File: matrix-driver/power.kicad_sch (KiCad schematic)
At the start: 28 parts, among them IC1 SPX5205M5-L-3-3_TR, U1 TPS562202, U3 TPS562202

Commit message: added gerbers and finalized v1.0
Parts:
- C12, C13: value 22uF -> 33uF
- C14: value 10nF -> 10pF; now not fitted
- C7: value 10nF -> 22pF
- IC1: DigiKey Part Number (none) -> 1016-1878-2-ND
- L1, L2: footprint (none) -> ETQ_P3M3R3KVP:IND_PCC-M0530M-LP_PAN
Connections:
- net +12V: now also C17.1, IC1.1 (VIN), IC1.3 (EN)

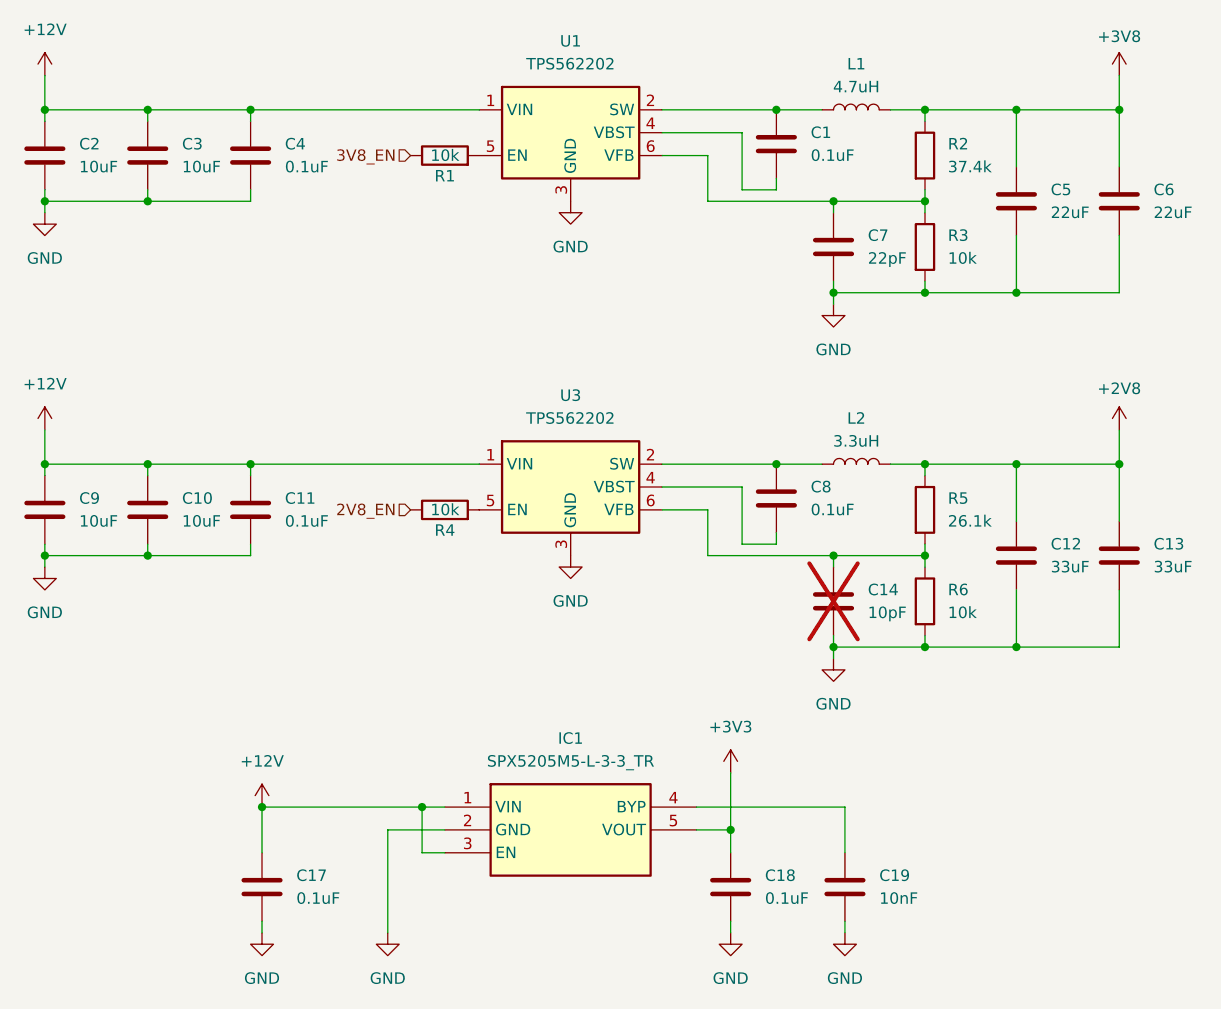
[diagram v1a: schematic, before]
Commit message: changed to through hole connectors for matrix drive unit and updated schematic to reflect thermistors and reserved pin
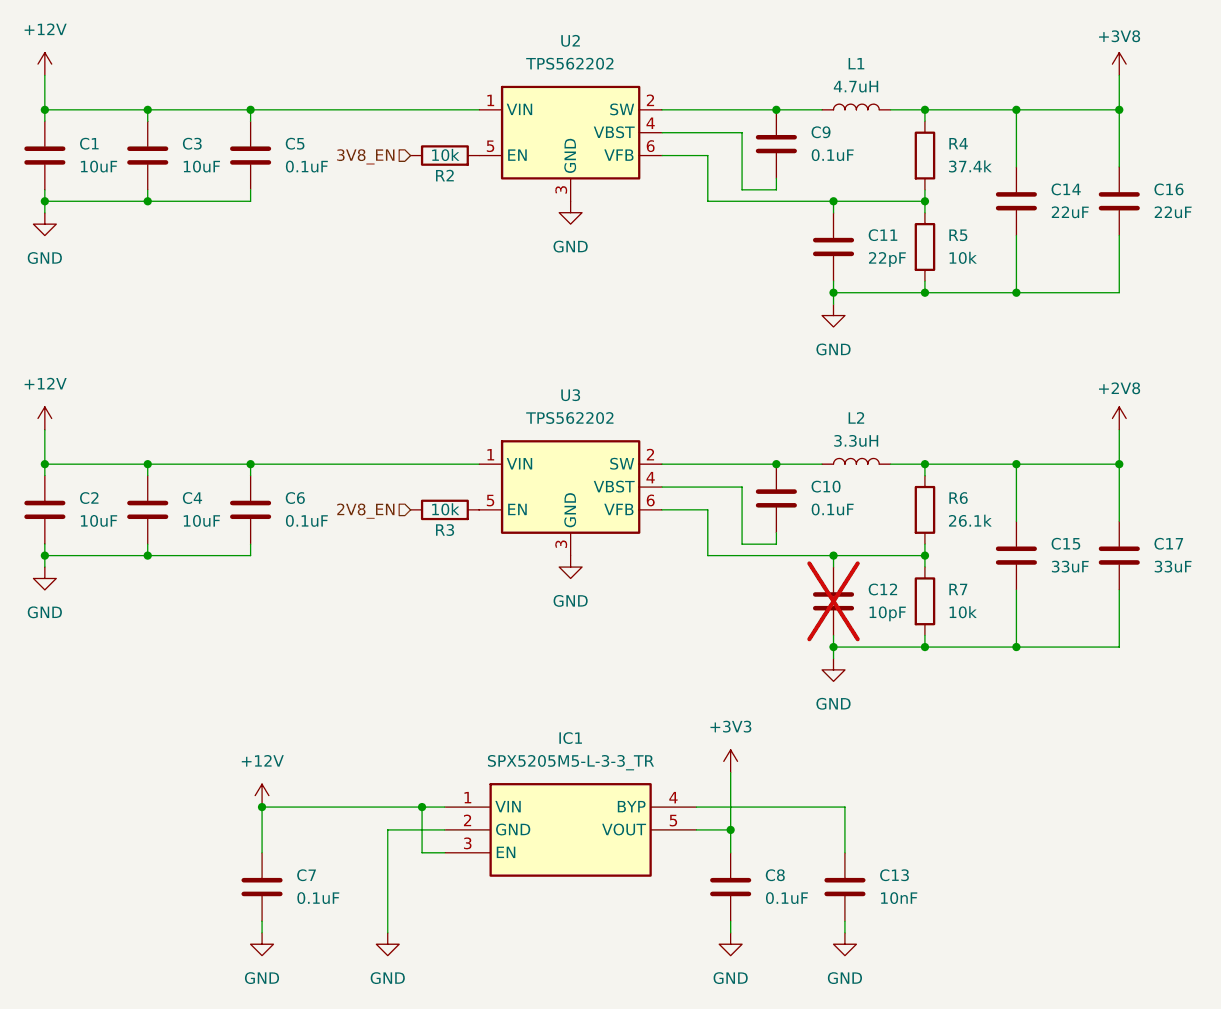
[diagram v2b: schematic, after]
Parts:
- renumbered C2 to C1, C8 to C10, C7 to C11, C14 to C12, C19 to C13, C5 to C14, C12 to C15, C6 to C16, C13 to C17, C9 to C2, C10 to C4, C4 to C5, C11 to C6, C17 to C7, C18 to C8, C1 to C9, R1 to R2, R4 to R3, R2 to R4, R3 to R5, R5 to R6, R6 to R7, U1 to U2
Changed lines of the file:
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@@
 		(dnp no)
 		(fields_autoplaced yes)
-		(property "Reference" "C2"
+		(property "Reference" "C1"
 			(at 91.44 53.3399 0)
 			(effects
@@
 			(project "matrix-driver"
 				(path "/7405d2be-e72b-4cfa-88bf-11e2906feea4/64d9626f-e1da-4cb3-b8ab-91f995897852"
-					(reference "C2")
+					(reference "C1")
 					(unit 1)
 				)
@@
 		(dnp no)
 		(fields_autoplaced yes)
-		(property "Reference" "R2"
+		(property "Reference" "R4"
 			(at 187.96 53.3399 0)
 			(effects
@@
 			(project "matrix-driver"
 				(path "/7405d2be-e72b-4cfa-88bf-11e2906feea4/64d9626f-e1da-4cb3-b8ab-91f995897852"
-					(reference "R2")
+					(reference "R4")
 					(unit 1)
 				)
@@
 		(dnp no)
 		(fields_autoplaced yes)
-		(property "Reference" "U1"
+		(property "Reference" "U2"
 			(at 146.05 41.91 0)
 			(effects
@@
 			(project "matrix-driver"
 				(path "/7405d2be-e72b-4cfa-88bf-11e2906feea4/64d9626f-e1da-4cb3-b8ab-91f995897852"
-					(reference "U1")
+					(reference "U2")
 					(unit 1)
 				)
@@
 		(dnp no)
 		(fields_autoplaced yes)
-		(property "Reference" "C6"
+		(property "Reference" "C16"
 			(at 210.82 58.4199 0)
 			(effects
@@
 			(project "matrix-driver"
 				(path "/7405d2be-e72b-4cfa-88bf-11e2906feea4/64d9626f-e1da-4cb3-b8ab-91f995897852"
-					(reference "C6")
+					(reference "C16")
 					(unit 1)
 				)
@@
 		(dnp no)
 		(fields_autoplaced yes)
-		(property "Reference" "C11"
+		(property "Reference" "C6"
 			(at 114.3 92.7099 0)
 			(effects
@@
 			(project "matrix-driver"
 				(path "/7405d2be-e72b-4cfa-88bf-11e2906feea4/64d9626f-e1da-4cb3-b8ab-91f995897852"
-					(reference "C11")
+					(reference "C6")
 					(unit 1)
 				)
@@
 		(on_board yes)
 		(dnp no)
-		(property "Reference" "R1"
+		(property "Reference" "R2"
 			(at 132.08 56.896 90)
 			(effects
@@
 			(project "matrix-driver"
 				(path "/7405d2be-e72b-4cfa-88bf-11e2906feea4/64d9626f-e1da-4cb3-b8ab-91f995897852"
-					(reference "R1")
+					(reference "R2")
 					(unit 1)
 				)
@@
 		(dnp no)
 		(fields_autoplaced yes)
-		(property "Reference" "C13"
+		(property "Reference" "C17"
 			(at 210.82 97.7899 0)
 			(effects
@@
 			(project "matrix-driver"
 				(path "/7405d2be-e72b-4cfa-88bf-11e2906feea4/64d9626f-e1da-4cb3-b8ab-91f995897852"
-					(reference "C13")
+					(reference "C17")
 					(unit 1)
 				)
@@
 		(dnp no)
 		(fields_autoplaced yes)
-		(property "Reference" "R5"
+		(property "Reference" "R6"
 			(at 187.96 92.7099 0)
 			(effects
@@
 			(project "matrix-driver"
 				(path "/7405d2be-e72b-4cfa-88bf-11e2906feea4/64d9626f-e1da-4cb3-b8ab-91f995897852"
-					(reference "R5")
+					(reference "R6")
 					(unit 1)
 				)
@@
 		(dnp no)
 		(fields_autoplaced yes)
-		(property "Reference" "C10"
+		(property "Reference" "C4"
 			(at 102.87 92.7099 0)
 			(effects
@@
 			(project "matrix-driver"
 				(path "/7405d2be-e72b-4cfa-88bf-11e2906feea4/64d9626f-e1da-4cb3-b8ab-91f995897852"
-					(reference "C10")
+					(reference "C4")
 					(unit 1)
 				)
@@
 		(dnp no)
 		(fields_autoplaced yes)
-		(property "Reference" "C1"
+		(property "Reference" "C9"
 			(at 172.72 52.0699 0)
 			(effects
@@
 			(project "matrix-driver"
 				(path "/7405d2be-e72b-4cfa-88bf-11e2906feea4/64d9626f-e1da-4cb3-b8ab-91f995897852"
-					(reference "C1")
+					(reference "C9")
 					(unit 1)
 				)
@@
 		(dnp no)
 		(fields_autoplaced yes)
-		(property "Reference" "C4"
+		(property "Reference" "C5"
 			(at 114.3 53.3399 0)
 			(effects
@@
 			(project "matrix-driver"
 				(path "/7405d2be-e72b-4cfa-88bf-11e2906feea4/64d9626f-e1da-4cb3-b8ab-91f995897852"
-					(reference "C4")
+					(reference "C5")
 					(unit 1)
 				)
@@
 		(dnp no)
 		(fields_autoplaced yes)
-		(property "Reference" "C7"
+		(property "Reference" "C11"
 			(at 179.07 63.4999 0)
 			(effects
@@
 			(project "matrix-driver"
 				(path "/7405d2be-e72b-4cfa-88bf-11e2906feea4/64d9626f-e1da-4cb3-b8ab-91f995897852"
-					(reference "C7")
+					(reference "C11")
 					(unit 1)
 				)
@@
 		(dnp no)
 		(fields_autoplaced yes)
-		(property "Reference" "C9"
+		(property "Reference" "C2"
 			(at 91.44 92.7099 0)
 			(effects
@@
 			(project "matrix-driver"
 				(path "/7405d2be-e72b-4cfa-88bf-11e2906feea4/64d9626f-e1da-4cb3-b8ab-91f995897852"
-					(reference "C9")
+					(reference "C2")
 					(unit 1)
 				)
@@
 		(dnp no)
 		(fields_autoplaced yes)
-		(property "Reference" "C19"
+		(property "Reference" "C13"
 			(at 180.34 134.6199 0)
 			(effects
@@
 			(project "matrix-driver"
 				(path "/7405d2be-e72b-4cfa-88bf-11e2906feea4/64d9626f-e1da-4cb3-b8ab-91f995897852"
-					(reference "C19")
+					(reference "C13")
 					(unit 1)
 				)
@@
 		(on_board yes)
 		(dnp no)
-		(property "Reference" "R4"
+		(property "Reference" "R3"
 			(at 132.08 96.266 90)
 			(effects
@@
 			(project "matrix-driver"
 				(path "/7405d2be-e72b-4cfa-88bf-11e2906feea4/64d9626f-e1da-4cb3-b8ab-91f995897852"
-					(reference "R4")
+					(reference "R3")
 					(unit 1)
 				)
@@
 		(dnp yes)
 		(fields_autoplaced yes)
-		(property "Reference" "C14"
+		(property "Reference" "C12"
 			(at 179.07 102.8699 0)
 			(effects
@@
 			(project "matrix-driver"
 				(path "/7405d2be-e72b-4cfa-88bf-11e2906feea4/64d9626f-e1da-4cb3-b8ab-91f995897852"
-					(reference "C14")
+					(reference "C12")
 					(unit 1)
 				)
@@
 		(dnp no)
 		(fields_autoplaced yes)
-		(property "Reference" "R6"
+		(property "Reference" "R7"
 			(at 187.96 102.8699 0)
 			(effects
@@
 			(project "matrix-driver"
 				(path "/7405d2be-e72b-4cfa-88bf-11e2906feea4/64d9626f-e1da-4cb3-b8ab-91f995897852"
-					(reference "R6")
+					(reference "R7")
 					(unit 1)
 				)
@@
 		(dnp no)
 		(fields_autoplaced yes)
-		(property "Reference" "C18"
+		(property "Reference" "C8"
 			(at 167.64 134.6199 0)
 			(effects
@@
 			(project "matrix-driver"
 				(path "/7405d2be-e72b-4cfa-88bf-11e2906feea4/64d9626f-e1da-4cb3-b8ab-91f995897852"
-					(reference "C18")
+					(reference "C8")
 					(unit 1)
 				)
@@
 		(dnp no)
 		(fields_autoplaced yes)
-		(property "Reference" "C5"
+		(property "Reference" "C14"
 			(at 199.39 58.4199 0)
 			(effects
@@
 			(project "matrix-driver"
 				(path "/7405d2be-e72b-4cfa-88bf-11e2906feea4/64d9626f-e1da-4cb3-b8ab-91f995897852"
-					(reference "C5")
+					(reference "C14")
 					(unit 1)
 				)
@@
 		(dnp no)
 		(fields_autoplaced yes)
-		(property "Reference" "R3"
+		(property "Reference" "R5"
 			(at 187.96 63.4999 0)
 			(effects
@@
 			(project "matrix-driver"
 				(path "/7405d2be-e72b-4cfa-88bf-11e2906feea4/64d9626f-e1da-4cb3-b8ab-91f995897852"
-					(reference "R3")
+					(reference "R5")
 					(unit 1)
 				)
@@
 		(dnp no)
 		(fields_autoplaced yes)
-		(property "Reference" "C8"
+		(property "Reference" "C10"
 			(at 172.72 91.4399 0)
 			(effects
@@
 			(project "matrix-driver"
 				(path "/7405d2be-e72b-4cfa-88bf-11e2906feea4/64d9626f-e1da-4cb3-b8ab-91f995897852"
-					(reference "C8")
+					(reference "C10")
 					(unit 1)
 				)
@@
 		(dnp no)
 		(fields_autoplaced yes)
-		(property "Reference" "C17"
+		(property "Reference" "C7"
 			(at 115.57 134.6199 0)
 			(effects
@@
 			(project "matrix-driver"
 				(path "/7405d2be-e72b-4cfa-88bf-11e2906feea4/64d9626f-e1da-4cb3-b8ab-91f995897852"
-					(reference "C17")
+					(reference "C7")
 					(unit 1)
 				)
@@
 		(dnp no)
 		(fields_autoplaced yes)
-		(property "Reference" "C12"
+		(property "Reference" "C15"
 			(at 199.39 97.7899 0)
 			(effects
@@
 			(project "matrix-driver"
 				(path "/7405d2be-e72b-4cfa-88bf-11e2906feea4/64d9626f-e1da-4cb3-b8ab-91f995897852"
-					(reference "C12")
+					(reference "C15")
 					(unit 1)
 				)
